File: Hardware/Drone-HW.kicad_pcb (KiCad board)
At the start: 2 copper layers, 61 x 40 mm, 26 parts, among them Con5 espTool_conn, J5 Conn_01x02_Pin, M1 pinH_2v, M2 pinH_2v, M3 pinH_2v, M4 pinH_2v, Q5 BC846, Q6 BC846, SW3 Tactile, U1 ESP32-WROOM-32D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

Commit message: Finalizando hardware aguardando revisão
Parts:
- added D1: LED, Local_LED_THT:LED_D1.8mm_W3.3mm_H2.4mm, F.Cu at (174.0, 56.0)
- added R1: 10k, Local_Resistor_SMD:R_0805_2012Metric_Pad1.15x1.40mm_HandSolder, F.Cu at (193.0, 59.0)
- added R2: 15k, Local_Resistor_SMD:R_0805_2012Metric_Pad1.15x1.40mm_HandSolder, F.Cu at (193.0, 63.0)
- added R3: 330, Local_Resistor_SMD:R_0805_2012Metric_Pad1.15x1.40mm_HandSolder, F.Cu at (170.0, 69.0)
- renumbered M1 to J1, M2 to J10, M3 to J2, M4 to J3
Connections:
- U1 pad 11: unconnected-(U1-IO26-Pad11) -> /V_Bat
- U1 pad 28: unconnected-(U1-IO17-Pad28) -> Net-(U1-IO17)
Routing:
- net /V_Bat: track 0.00 -> 93.4 mm, vias 0 -> 2
- net +7V4: track 16.4 -> 53.5 mm
- net Net-(U1-IO17): track 0.00 -> 31.7 mm, vias 0 -> 2
- net Net-(D1-A): track 0.00 -> 24.2 mm, vias 0 -> 1
- net GND: track 1.44 -> 4.05 mm, vias 32 -> 34
- net /Motor2: track 41.7 -> 42.4 mm
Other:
- board text added: "AEROMÃO-AFJPP v20250903"
- board text removed: ":D AEROMÃO-AFJPP v20250903"

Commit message: Arrumando hardware
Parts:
- removed J10: pinH_2v, Local_Connector_PinHeader_2.54mm:PinHeader_1x02_P2.54mm_Vertical
- added J4: Conn_01x03, Connector_PinHeader_2.00mm:PinHeader_1x03_P2.00mm_Vertical, F.Cu at (144.5, 68.5)
- J1, J2, J3: value pinH_2v -> Conn_01x03; footprint Local_Connector_PinHeader_2.54mm:PinHeader_1x02_P2.54mm_Vertical -> Connector_PinHeader_2.00mm:PinHeader_1x03_P2.00mm_Vertical
- R3: value 330 -> 470R
- U1: footprint Local_RF_Module:ESP32-WROOM-32_PRODIGITAL -> RF_Module:ESP32-WROOM-32U
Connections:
- D1 pad 1: GND -> Net-(D1-K)
- J2 pad 1: /Motor3 -> /Motor2
- J3 pad 1: /Motor4 -> /Motor3
- R3 pad 1: Net-(D1-A) -> +3V3
- R3 pad 2: Net-(U1-IO17) -> Net-(D1-A)
- U1 pad 10: unconnected-(U1-IO25-Pad10) -> /sw4
- U1 pad 14: unconnected-(U1-IO12(SPD)-Pad14) -> /sw2
- U1 pad 23: unconnected-(U1-IO15(SPU)-Pad23) -> /sw3
- U1 pad 28: Net-(U1-IO17) -> Net-(D1-K)
- U1 pad 29: unconnected-(U1-IO5(SPU)-Pad29) -> /sw1
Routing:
- net /sw3: track 0.00 -> 75.3 mm, vias 0 -> 3
- net /sw4: track 0.00 -> 63.1 mm, vias 0 -> 1
- net /sw1: track 0.00 -> 54.8 mm, vias 0 -> 1
- net /sw2: track 0.00 -> 36.5 mm, vias 0 -> 1
- net Net-(U1-IO17): track 31.7 -> 0.00 mm, vias 2 -> 0
- net Net-(D1-A): track 24.2 -> 56.0 mm, vias 1 -> 3
- net /V_Bat: track 93.4 -> 95.7 mm
- net /MISO: track 39.8 -> 41.6 mm
- net GND: vias 34 -> 37
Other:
- board size 61 x 40 mm -> 61 x 41 mm

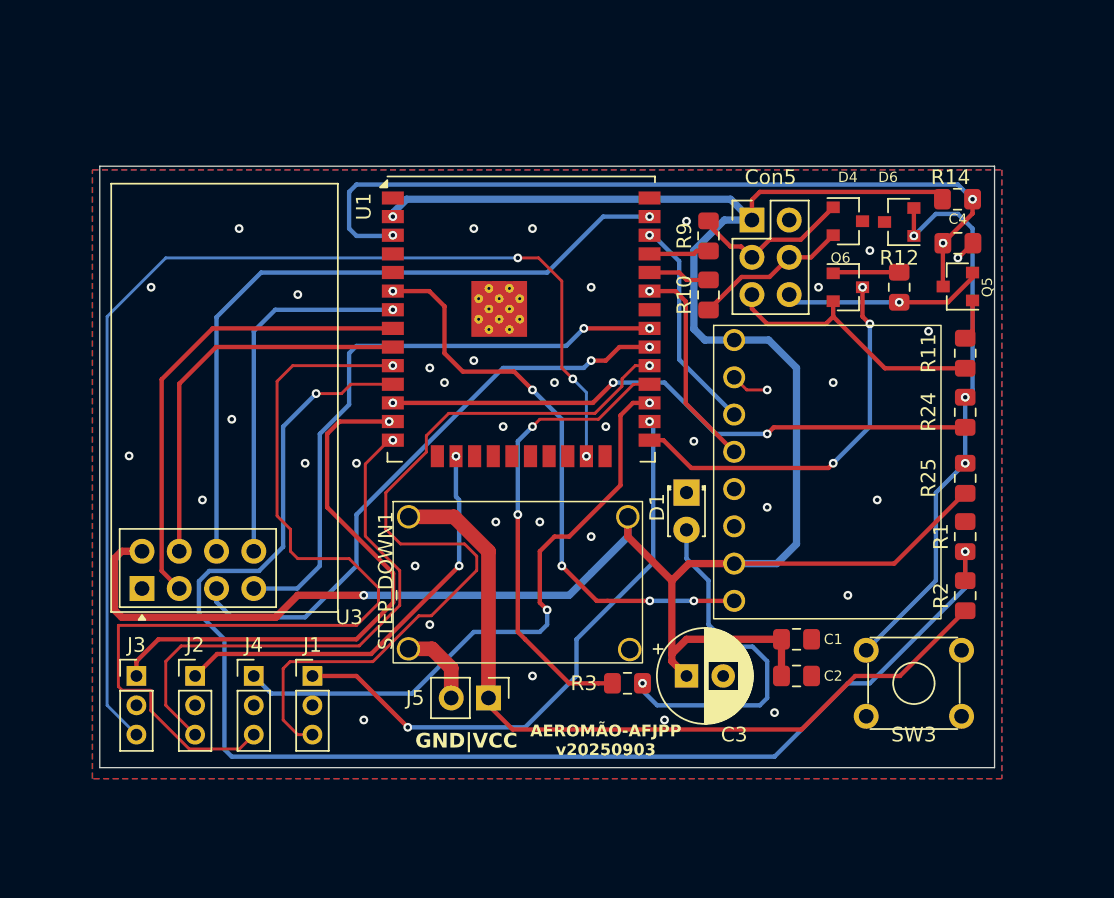
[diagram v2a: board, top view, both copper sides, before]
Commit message: Arrumando erros de DRC hw
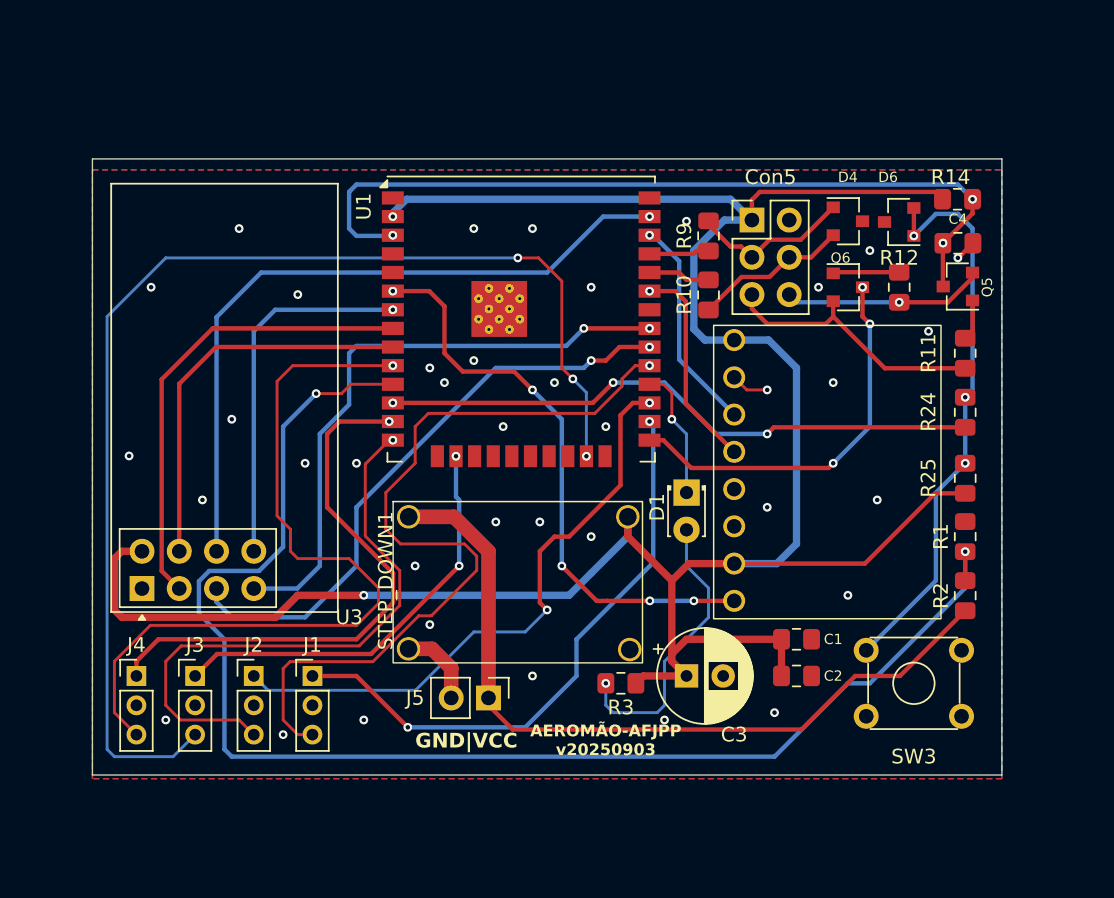
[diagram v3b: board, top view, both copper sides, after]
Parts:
- moved J4 8.00 mm to (136.5, 68.5)
- moved J2 4.00 mm to (144.5, 68.5)
- moved J3 4.00 mm to (140.5, 68.5)
- moved R3 0.45 mm to (169.5, 69.0)
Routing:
- net Net-(D1-A): track 56.0 -> 19.7 mm, vias 3 -> 1
- net /sw4: track 63.1 -> 53.6 mm
- net Net-(D1-K): track 0.00 -> 8.99 mm, vias 0 -> 1
- net /sw3: track 75.3 -> 82.3 mm
- net /sw2: track 36.5 -> 40.5 mm
- net +3V3: track 165.7 -> 169.3 mm
- net /sw1: track 54.8 -> 55.6 mm
- net /Motor2: track 42.1 -> 41.3 mm
- net GND: vias 37 -> 38
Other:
- board size 61 x 41 mm -> 62 x 42 mm

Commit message: alteracoes finais
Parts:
- moved SW3 1.58 mm to (185.8, 68.2)
- moved R3 1.50 mm to (169.5, 70.5)
- moved Q6 1.50 mm to (186.5, 42.0)
- moved R10 1.14 mm to (175.0, 41.5)
- moved R9 1.14 mm to (175.0, 37.5)
- moved C2 1.11 mm to (180.5, 69.0), turned to -90 degrees
- moved R12 1.00 mm to (189.5, 42.0)
- moved R14 0.53 mm to (193.0, 36.0)
- moved C4 0.50 mm to (193.0, 39.0)
- moved D4 0.50 mm to (185.5, 37.5)
- moved D6 0.50 mm to (189.0, 37.5)
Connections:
- Con5 pad 1: +3V3 -> unconnected-(Con5-3v3-Pad1)
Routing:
- net +7V4: track 53.5 -> 55.5 mm
- net Net-(D6-A2): track 38.7 -> 40.3 mm, vias 3 -> 4
- net GND: track 4.05 -> 2.61 mm, vias 38 -> 36
- net +3V3: track 169.3 -> 167.9 mm, vias 2 -> 3
- net /RTS_ESP: track 13.8 -> 14.7 mm
- net Net-(Con5-TX): track 11.4 -> 12.3 mm
- net /EN_ESP: track 55.6 -> 56.4 mm
- net /V_Bat: track 95.7 -> 96.3 mm
- net Net-(Con5-RX): track 10.6 -> 11.2 mm
- net /SDA-SPU: track 14.4 -> 13.8 mm
- net Net-(Q6-B): track 4.53 -> 4.03 mm
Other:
- board size 62 x 42 mm -> 62.5 x 42 mm

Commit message: Dando push na versão final de hardware
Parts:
- added H1: MountingHole, MountingHole:MountingHole_2.1mm, F.Cu at (137.2, 32.2)
- added H2: MountingHole, MountingHole:MountingHole_2.1mm, F.Cu at (191.3, 31.9)
- added H3: MountingHole, MountingHole:MountingHole_2.1mm, F.Cu at (190.8, 76.5)
- added H4: MountingHole, MountingHole:MountingHole_2.1mm, F.Cu at (137.2, 76.5)
- moved J1 49.1 mm to (181.2, 31.9), turned to 90 degrees
- moved J3 40.2 mm to (179.7, 77.3), turned to 90 degrees
- moved J2 36.3 mm to (144.3, 32.2), turned to 90 degrees
- moved J4 10.5 mm to (141.9, 77.5), turned to 90 degrees
- moved STEP_DOWN1 0.09 mm to (153.9, 56.6)
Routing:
- net /sw3: track 82.3 -> 41.6 mm, vias 3 -> 2
- net /sw1: track 55.6 -> 31.7 mm, vias 1 -> 2
- net /sw2: track 40.5 -> 22.8 mm, vias 1 -> 2
- net /Motor3: track 28.7 -> 40.9 mm
- net /MISO: track 41.6 -> 35.3 mm, vias 2 -> 1
- net /Motor1: track 40.5 -> 35.5 mm
- net /sw4: track 53.6 -> 50.6 mm, vias 1 -> 3
- net /Motor4: track 38.1 -> 35.4 mm, vias 1 -> 0
- net /Motor2: track 41.3 -> 43.4 mm, vias 2 -> 0
- net /V_Bat: track 96.3 -> 97.5 mm
- net /SCK: track 40.8 -> 39.7 mm, vias 2 -> 1
- net /B_START: track 41.2 -> 40.5 mm, vias 3 -> 2
- net /IRQ: track 25.1 -> 25.6 mm
- net GND: vias 36 -> 33
- net /SDA-SPU: vias 1 -> 0
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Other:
- board size 62.5 x 42 mm -> 61.7 x 50.5 mm
- board text added: "AEROMÃO-AFJPP v20251012"
- board text added: "M - GND - SW"
- board text removed: "AEROMÃO-AFJPP v20250903"
